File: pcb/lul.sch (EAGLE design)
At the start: 79 parts, among them IC1 STM32F072C8T6, IC2 REG1117, IC3 74LVC1G125DBV, U1 UG-2864HSWEG01, X1 USB-MICROB

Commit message: adjusted position of led cap
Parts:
- added U$10, U$11, U$12, U$13, U$14, U$7, U$9: M3_MOUNTING_HOLE, clock:M3_MOUNTING_HOLE
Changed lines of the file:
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@@
 <part name="TP1" library="clock" deviceset="TEST-POINT" device="3X5"/>
 <part name="TP2" library="clock" deviceset="TEST-POINT" device="3X5"/>
+<part name="U$7" library="clock" deviceset="M3_MOUNTING_HOLE" device=""/>
+<part name="U$9" library="clock" deviceset="M3_MOUNTING_HOLE" device=""/>
+<part name="U$10" library="clock" deviceset="M3_MOUNTING_HOLE" device=""/>
+<part name="U$11" library="clock" deviceset="M3_MOUNTING_HOLE" device=""/>
+<part name="U$12" library="clock" deviceset="M3_MOUNTING_HOLE" device=""/>
+<part name="U$13" library="clock" deviceset="M3_MOUNTING_HOLE" device=""/>
+<part name="U$14" library="clock" deviceset="M3_MOUNTING_HOLE" device=""/>
 </parts>
 <sheets>
@@
 <instance part="TP1" gate="G$1" x="-73.66" y="30.48" smashed="yes" rot="R90"/>
 <instance part="TP2" gate="G$1" x="-40.64" y="30.48" smashed="yes" rot="R90"/>
+<instance part="U$7" gate="G$1" x="474.98" y="38.1"/>
+<instance part="U$9" gate="G$1" x="515.62" y="35.56"/>
+<instance part="U$10" gate="G$1" x="464.82" y="12.7"/>
+<instance part="U$11" gate="G$1" x="528.32" y="10.16"/>
+<instance part="U$12" gate="G$1" x="497.84" y="-5.08"/>
+<instance part="U$13" gate="G$1" x="485.14" y="25.4"/>
+<instance part="U$14" gate="G$1" x="472.44" y="-5.08"/>
 </instances>
 <busses>

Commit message: v1
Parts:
- added U$15, U$16: M3_MOUNTING_HOLE, clock:M3_MOUNTING_HOLE
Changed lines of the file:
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@@
 <part name="U$13" library="clock" deviceset="M3_MOUNTING_HOLE" device=""/>
 <part name="U$14" library="clock" deviceset="M3_MOUNTING_HOLE" device=""/>
+<part name="U$15" library="clock" deviceset="M3_MOUNTING_HOLE" device=""/>
+<part name="U$16" library="clock" deviceset="M3_MOUNTING_HOLE" device=""/>
 </parts>
 <sheets>
@@
 <instance part="U$13" gate="G$1" x="485.14" y="25.4"/>
 <instance part="U$14" gate="G$1" x="472.44" y="-5.08"/>
+<instance part="U$15" gate="G$1" x="482.6" y="27.94"/>
+<instance part="U$16" gate="G$1" x="500.38" y="10.16"/>
 </instances>
 <busses>

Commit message: RTOS working start
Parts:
- C3, C4, C6, C7: value 1uF -> 2.2uF
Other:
- note added: "1uF for 0.96 inch 2.2uF for 1.3 inch"
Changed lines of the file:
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@@
 <part name="U$2" library="supply1" library_urn="urn:adsk.eagle:library:371" deviceset="GND" device=""/>
 <part name="R3" library="clock" deviceset="RESISTOR" device="0805-RES" value="390K"/>
-<part name="C3" library="clock" deviceset="CAP" device="0805" value="1uF"/>
-<part name="C4" library="clock" deviceset="CAP" device="0805" value="1uF"/>
+<part name="C3" library="clock" deviceset="CAP" device="0805" value="2.2uF"/>
+<part name="C4" library="clock" deviceset="CAP" device="0805" value="2.2uF"/>
 <part name="U$18" library="supply1" library_urn="urn:adsk.eagle:library:371" deviceset="GND" device=""/>
 <part name="U$19" library="supply1" library_urn="urn:adsk.eagle:library:371" deviceset="GND" device=""/>
 <part name="C5" library="clock" deviceset="CAP" device="0805" value="10uF"/>
 <part name="U$20" library="supply1" library_urn="urn:adsk.eagle:library:371" deviceset="GND" device=""/>
-<part name="C7" library="clock" deviceset="CAP" device="0805" value="1uF"/>
+<part name="C7" library="clock" deviceset="CAP" device="0805" value="2.2uF"/>
 <part name="C8" library="clock" deviceset="CAP" device="0805" value="2.2uF/16V"/>
 <part name="U$21" library="supply1" library_urn="urn:adsk.eagle:library:371" deviceset="GND" device=""/>
-<part name="C6" library="clock" deviceset="CAP" device="0805" value="1uF"/>
+<part name="C6" library="clock" deviceset="CAP" device="0805" value="2.2uF"/>
 <part name="IC1" library="clock" deviceset="STM32F072C8T6" device=""/>
 <part name="SD1" library="clock" deviceset="TF-HOLDER" device=""/>
@@
 <sheet>
 <plain>
+<text x="297.18" y="63.5" size="1.778" layer="97">1uF for 0.96 inch
+2.2uF for 1.3 inch </text>
 </plain>
 <instances>
@@
 </drawing>
 <compatibility>
+<note version="6.3" minversion="6.2.2" severity="warning">
+Since Version 6.2.2 text objects can contain more than one line,
+which will not be processed correctly with this version.
+</note>
 <note version="8.2" severity="warning">
 Since Version 8.2, Eagle supports online libraries. The ids

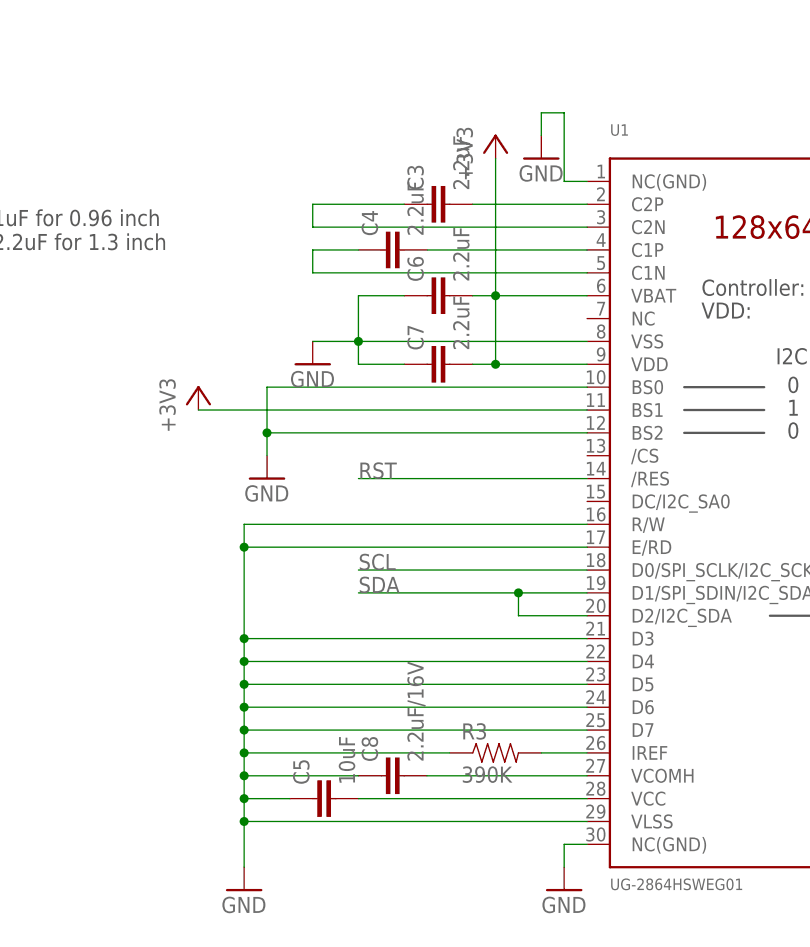
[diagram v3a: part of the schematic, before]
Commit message: changed cap values
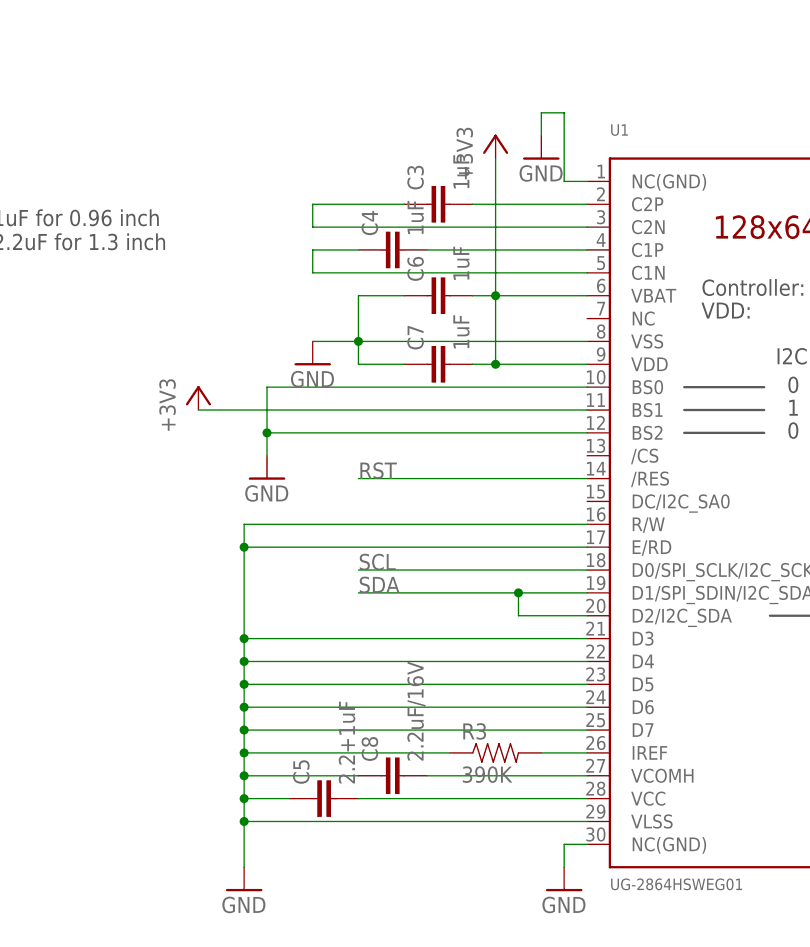
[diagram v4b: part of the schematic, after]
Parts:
- C3, C4, C6, C7: value 2.2uF -> 1uF
- C5: value 10uF -> 2.2+1uF
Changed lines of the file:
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@@
 <part name="U$2" library="supply1" library_urn="urn:adsk.eagle:library:371" deviceset="GND" device=""/>
 <part name="R3" library="clock" deviceset="RESISTOR" device="0805-RES" value="390K"/>
-<part name="C3" library="clock" deviceset="CAP" device="0805" value="2.2uF"/>
-<part name="C4" library="clock" deviceset="CAP" device="0805" value="2.2uF"/>
+<part name="C3" library="clock" deviceset="CAP" device="0805" value="1uF"/>
+<part name="C4" library="clock" deviceset="CAP" device="0805" value="1uF"/>
 <part name="U$18" library="supply1" library_urn="urn:adsk.eagle:library:371" deviceset="GND" device=""/>
 <part name="U$19" library="supply1" library_urn="urn:adsk.eagle:library:371" deviceset="GND" device=""/>
-<part name="C5" library="clock" deviceset="CAP" device="0805" value="10uF"/>
+<part name="C5" library="clock" deviceset="CAP" device="0805" value="2.2+1uF"/>
 <part name="U$20" library="supply1" library_urn="urn:adsk.eagle:library:371" deviceset="GND" device=""/>
-<part name="C7" library="clock" deviceset="CAP" device="0805" value="2.2uF"/>
+<part name="C7" library="clock" deviceset="CAP" device="0805" value="1uF"/>
 <part name="C8" library="clock" deviceset="CAP" device="0805" value="2.2uF/16V"/>
 <part name="U$21" library="supply1" library_urn="urn:adsk.eagle:library:371" deviceset="GND" device=""/>
-<part name="C6" library="clock" deviceset="CAP" device="0805" value="2.2uF"/>
+<part name="C6" library="clock" deviceset="CAP" device="0805" value="1uF"/>
 <part name="IC1" library="clock" deviceset="STM32F072C8T6" device=""/>
 <part name="SD1" library="clock" deviceset="TF-HOLDER" device=""/>

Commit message: new pcb layout for oled reset
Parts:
- removed R1: 10k, clock:RESISTOR0805-RES
- removed TP1, TP2: TEST-POINT3X5, clock:TEST-POINT3X5
- removed U$8: TEMT6000, ProtoSnap-v14a:TEMT6000
- added R7, R8: 4K7, clock:RESISTOR0805-RES
- IC3: value 74LVC1G125DBV -> 74AHCT1G08DBV; device 74xx-little-de:74LVC1G125DBV -> 74xx-little-de:74AHCT1G08DBV
- R3: value 390K -> 560K
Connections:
- removed net LIGHT_SENSOR_OUTPUT: IC1PORTA_L.PA2, R17.2, U$8.E1
- new net OLED_RESET: IC1PORTA_L.PA2, R17.2, U1./RES
- net +3V3: now also R7.2, R8.2; no longer R5.2, U$8.C1
- net GND: now also R5.1, U1./CS, U1.DC/I2C_SA0, U1.NC; no longer R1.1
- net LED_DATA_EN: now also IC3A.I0, R5.2; no longer IC3A.OE, R5.1
- net N$29: no longer R1.2, TP1.1
- net RST: no longer U1./RES
- net SCL: now also R7.1
- net SDA: now also R8.1
- net SPI_MOSI: now also IC3A.I1; no longer IC3A.I, TP2.1
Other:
- note removed: "1uF for 0.96 inch 2.2uF for 1.3 inch"
- moved on the sheet: IC3P, R17, R5

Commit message: cleaned up schematics
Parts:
- C5: value 2.2+1uF -> 2.2uF
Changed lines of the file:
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@@
 <?xml version="1.0" encoding="utf-8"?>
 <!DOCTYPE eagle SYSTEM "eagle.dtd">
-<eagle version="8.2.2">
+<eagle version="8.3.2">
 <drawing>
 <settings>
 <setting alwaysvectorfont="yes"/>
+<setting keepoldvectorfont="yes"/>
 <setting verticaltext="up"/>
 </settings>
@@
 <part name="U$18" library="supply1" library_urn="urn:adsk.eagle:library:371" deviceset="GND" device=""/>
 <part name="U$19" library="supply1" library_urn="urn:adsk.eagle:library:371" deviceset="GND" device=""/>
-<part name="C5" library="clock" deviceset="CAP" device="0805" value="2.2+1uF"/>
+<part name="C5" library="clock" deviceset="CAP" device="0805" value="2.2uF"/>
 <part name="U$20" library="supply1" library_urn="urn:adsk.eagle:library:371" deviceset="GND" device=""/>
 <part name="C7" library="clock" deviceset="CAP" device="0805" value="1uF"/>
@@
 <instance part="LED14" gate="G$1" x="-137.16" y="-121.92" rot="MR0"/>
 <instance part="LED15" gate="G$1" x="-96.52" y="-121.92" rot="MR0"/>
-<instance part="+3V11" gate="G$1" x="-180.34" y="43.18" rot="MR0"/>
-<instance part="+3V12" gate="G$1" x="-132.08" y="43.18" rot="MR0"/>
-<instance part="+3V13" gate="G$1" x="-88.9" y="43.18" rot="MR0"/>
+<instance part="+3V11" gate="G$1" x="-190.5" y="43.18" rot="MR0"/>
+<instance part="+3V12" gate="G$1" x="-142.24" y="43.18" rot="MR0"/>
+<instance part="+3V13" gate="G$1" x="-99.06" y="43.18" rot="MR0"/>
 <instance part="+3V14" gate="G$1" x="-88.9" y="7.62" rot="MR0"/>
 <instance part="+3V15" gate="G$1" x="-132.08" y="7.62" rot="MR0"/>
 <instance part="+3V16" gate="G$1" x="-180.34" y="7.62" rot="MR0"/>
-<instance part="+3V17" gate="G$1" x="-180.34" y="-30.48" rot="MR0"/>
-<instance part="+3V18" gate="G$1" x="-132.08" y="-30.48" rot="MR0"/>
-<instance part="+3V19" gate="G$1" x="-88.9" y="-30.48" rot="MR0"/>
+<instance part="+3V17" gate="G$1" x="-190.5" y="-30.48" rot="MR0"/>
+<instance part="+3V18" gate="G$1" x="-142.24" y="-30.48" rot="MR0"/>
+<instance part="+3V19" gate="G$1" x="-99.06" y="-30.48" rot="MR0"/>
 <instance part="+3V20" gate="G$1" x="-88.9" y="-71.12" rot="MR0"/>
 <instance part="+3V21" gate="G$1" x="-132.08" y="-71.12" rot="MR0"/>
 <instance part="+3V22" gate="G$1" x="-180.34" y="-71.12" rot="MR0"/>
-<instance part="+3V23" gate="G$1" x="-180.34" y="-104.14" rot="MR0"/>
-<instance part="+3V24" gate="G$1" x="-132.08" y="-104.14" rot="MR0"/>
-<instance part="+3V25" gate="G$1" x="-91.44" y="-104.14" rot="MR0"/>
+<instance part="+3V23" gate="G$1" x="-190.5" y="-104.14" rot="MR0"/>
+<instance part="+3V24" gate="G$1" x="-142.24" y="-104.14" rot="MR0"/>
+<instance part="+3V25" gate="G$1" x="-101.6" y="-104.14" rot="MR0"/>
 <instance part="GND2" gate="1" x="-96.52" y="-134.62"/>
 <instance part="GND3" gate="1" x="-137.16" y="-134.62"/>
@@
 <instance part="+3V32" gate="G$1" x="-63.5" y="63.5" rot="MR0"/>
 <instance part="C27" gate="G$1" x="-238.76" y="-35.56"/>
-<instance part="U$7" gate="G$1" x="474.98" y="38.1"/>
-<instance part="U$9" gate="G$1" x="515.62" y="35.56"/>
-<instance part="U$10" gate="G$1" x="464.82" y="12.7"/>
-<instance part="U$11" gate="G$1" x="528.32" y="10.16"/>
-<instance part="U$12" gate="G$1" x="497.84" y="-5.08"/>
-<instance part="U$13" gate="G$1" x="485.14" y="25.4"/>
-<instance part="U$14" gate="G$1" x="472.44" y="-5.08"/>
-<instance part="U$15" gate="G$1" x="482.6" y="27.94"/>
-<instance part="U$16" gate="G$1" x="500.38" y="10.16"/>
+<instance part="U$7" gate="G$1" x="467.36" y="48.26"/>
+<instance part="U$9" gate="G$1" x="495.3" y="15.24"/>
+<instance part="U$10" gate="G$1" x="467.36" y="33.02"/>
+<instance part="U$11" gate="G$1" x="523.24" y="33.02"/>
+<instance part="U$12" gate="G$1" x="523.24" y="15.24"/>
+<instance part="U$13" gate="G$1" x="495.3" y="33.02"/>
+<instance part="U$14" gate="G$1" x="467.36" y="15.24"/>
+<instance part="U$15" gate="G$1" x="495.3" y="48.26"/>
+<instance part="U$16" gate="G$1" x="523.24" y="48.26"/>
 <instance part="R7" gate="G$1" x="299.72" y="33.02" rot="R90"/>
 <instance part="R8" gate="G$1" x="292.1" y="30.48" rot="R90"/>
@@
 <pinref part="LED1" gate="G$1" pin="VDD"/>
 <pinref part="+3V11" gate="G$1" pin="+3V3"/>
-<wire x1="-190.5" y1="40.64" x2="-180.34" y2="40.64" width="0.1524" layer="91"/>
 </segment>
 <segment>
 <pinref part="LED2" gate="G$1" pin="VDD"/>
 <pinref part="+3V12" gate="G$1" pin="+3V3"/>
-<wire x1="-142.24" y1="40.64" x2="-132.08" y2="40.64" width="0.1524" layer="91"/>
 </segment>
 <segment>
 <pinref part="LED3" gate="G$1" pin="VDD"/>
 <pinref part="+3V13" gate="G$1" pin="+3V3"/>
-<wire x1="-99.06" y1="40.64" x2="-88.9" y2="40.64" width="0.1524" layer="91"/>
 </segment>
 <segment>
@@
 <pinref part="LED7" gate="G$1" pin="VDD"/>
 <pinref part="+3V17" gate="G$1" pin="+3V3"/>
-<wire x1="-190.5" y1="-33.02" x2="-180.34" y2="-33.02" width="0.1524" layer="91"/>
 </segment>
 <segment>
 <pinref part="LED8" gate="G$1" pin="VDD"/>
 <pinref part="+3V18" gate="G$1" pin="+3V3"/>
-<wire x1="-142.24" y1="-33.02" x2="-132.08" y2="-33.02" width="0.1524" layer="91"/>
 </segment>
 <segment>
 <pinref part="LED9" gate="G$1" pin="VDD"/>
 <pinref part="+3V19" gate="G$1" pin="+3V3"/>
-<wire x1="-99.06" y1="-33.02" x2="-88.9" y2="-33.02" width="0.1524" layer="91"/>
 </segment>
 <segment>
@@
 <pinref part="LED13" gate="G$1" pin="VDD"/>
 <pinref part="+3V23" gate="G$1" pin="+3V3"/>
-<wire x1="-190.5" y1="-106.68" x2="-180.34" y2="-106.68" width="0.1524" layer="91"/>
 </segment>
 <segment>
 <pinref part="LED14" gate="G$1" pin="VDD"/>
 <pinref part="+3V24" gate="G$1" pin="+3V3"/>
-<wire x1="-142.24" y1="-106.68" x2="-132.08" y2="-106.68" width="0.1524" layer="91"/>
 </segment>
 <segment>
 <pinref part="LED15" gate="G$1" pin="VDD"/>
 <pinref part="+3V25" gate="G$1" pin="+3V3"/>
-<wire x1="-101.6" y1="-106.68" x2="-91.44" y2="-106.68" width="0.1524" layer="91"/>
 </segment>
 <segment>
@@
 <compatibility>
 <note version="8.2" severity="warning">
-Since Version 8.2, Eagle supports online libraries. The ids
+Since Version 8.2, EAGLE supports online libraries. The ids
 of those online libraries will not be understood (or retained)
 with this version.

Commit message: writing README
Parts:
- C27: value (none) -> 47uF
- R17: value (none) -> 10K
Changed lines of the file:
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@@
 <part name="U$3" library="supply1" library_urn="urn:adsk.eagle:library:371" deviceset="GND" device=""/>
 <part name="+3V2" library="supply1" library_urn="urn:adsk.eagle:library:371" deviceset="+3V3" device=""/>
-<part name="R17" library="clock" deviceset="RESISTOR" device="0805-RES"/>
+<part name="R17" library="clock" deviceset="RESISTOR" device="0805-RES" value="10K"/>
 <part name="GND45" library="backplane" deviceset="GND" device=""/>
 <part name="GND19" library="supply1" library_urn="urn:adsk.eagle:library:371" deviceset="GND" device=""/>
@@
 <part name="GND32" library="supply1" library_urn="urn:adsk.eagle:library:371" deviceset="GND" device=""/>
 <part name="+3V32" library="supply1" library_urn="urn:adsk.eagle:library:371" deviceset="+3V3" device=""/>
-<part name="C27" library="clock" deviceset="C-US" device="C1210"/>
+<part name="C27" library="clock" deviceset="C-US" device="C1210" value="47uF"/>
 <part name="U$7" library="clock" deviceset="M3_MOUNTING_HOLE" device=""/>
 <part name="U$9" library="clock" deviceset="M3_MOUNTING_HOLE" device=""/>
